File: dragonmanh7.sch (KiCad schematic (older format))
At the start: 145 parts, among them J1 USB_B, J10 Conn_02x12_Odd_Even, J11 Conn_02x05_Odd_Even, J12 VBAT+, J13 Conn_02x05_Odd_Even, J14 VBATG, J15 Conn_02x02_Odd_Even, J16 Conn_02x02_Odd_Even, J18 Conn_02x05_Odd_Even, J2 73725-0110BLF, J3 RJ45_Amphenol_RJMG1BD3B8K1ANR, J4 105162-0001, J5 Screw_Terminal_01x06, J6 Conn_02x12_Odd_Even, J7 USB_B, J8 Screw_Terminal_01x02, J9 Conn_02x12_Odd_Even, SW1 RESET, SW2 PC13, U1 STM32H743VITx, U10 USBLC6-2SC6, U12 TCAN332, U13 ISL83483, U14 MIC2005A, U2 LAN8742A-CZ-TR, U3 AZ1117CD-3.3TRG1, U5 S25FL127SABMFI101, U6 AP63205, U7 USBLC6-2SC6, U8 STM32F042F6Px, U9 USBLC6-2SC6, Y1 8MHz, Y2 32.768KHz, Y3 25MHz

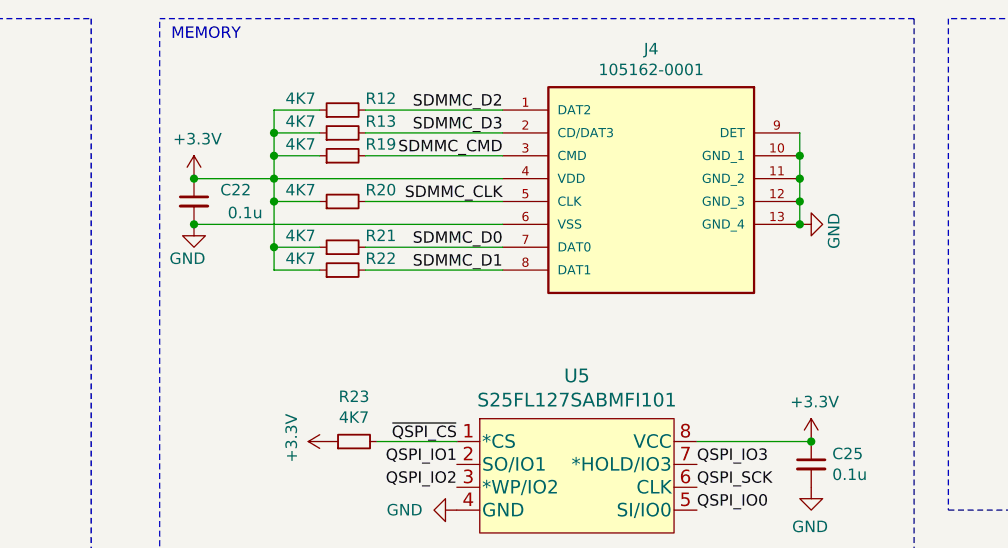
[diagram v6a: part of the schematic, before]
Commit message: Add ESD filters to uSD connector, improve routing
Signed-off-by: Martin Ribelotta <martinribelotta@gmail.com>
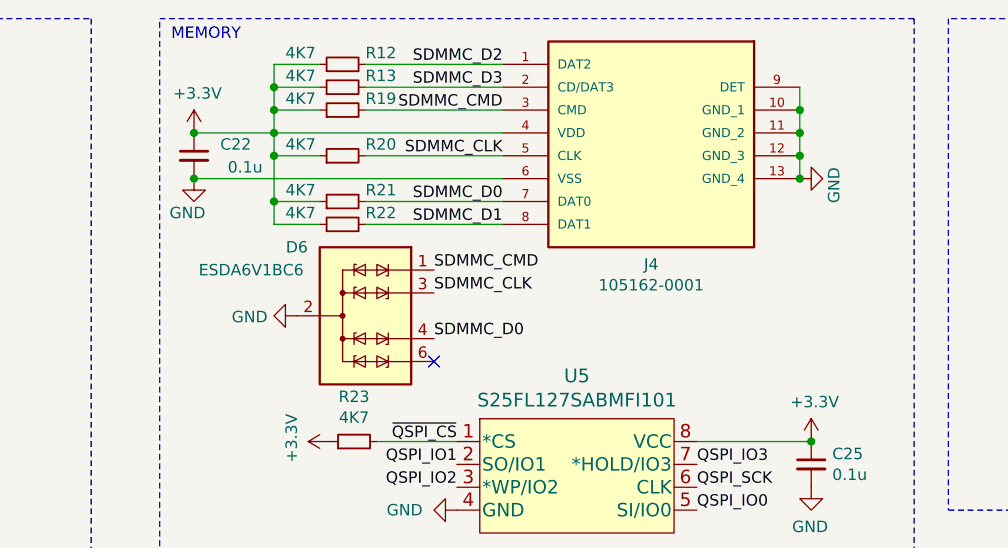
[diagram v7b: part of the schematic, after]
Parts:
- added D6: ESDA6V1BC6, Package_TO_SOT_SMD:SOT-23-6, symbol Power_Protection:ESDA6V1BC6
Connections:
- net GND: now also D6.2 (COM), D6.5 (COM)
- net SDMMC_CLK: now also D6.3 (TVS2)
- net SDMMC_CMD: now also D6.1 (TVS1)
- net SDMMC_D0: now also D6.4 (TVS3)
- no-connect marks 6 -> 7
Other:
- moved on the sheet: C22, J4, R12, R13, R19, R20, R21, R22
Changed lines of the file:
@@
 Text Label 1950 5150 2    50   ~ 0
 SDMMC_CMD
-Text Label 6550 1150 2    50   ~ 0
+Text Label 6550 950  2    50   ~ 0
 SDMMC_CMD
-Text Label 6550 1550 2    50   ~ 0
-SDMMC_D0
 Text Label 6550 1350 2    50   ~ 0
+SDMMC_D0
+Text Label 6550 1150 2    50   ~ 0
 SDMMC_CLK
 $Comp
 L Device:C_Small C22
 U 1 1 5C63370C
-P 5200 1350
-F 0 "C22" H 4950 1400 50  0000 L CNN
-F 1 "0.1u" H 4900 1300 50  0000 L CNN
-F 2 "Capacitor_SMD:C_0603_1608Metric" H 5200 1350 50  0001 C CNN
-F 3 "~" H 5200 1350 50  0001 C CNN
-F 4 "885012207098" H -300 0   50  0001 C CNN "manf#"
-	1    5200 1350
+P 5200 1150
+F 0 "C22" H 4950 1200 50  0000 L CNN
+F 1 "0.1u" H 4900 1100 50  0000 L CNN
+F 2 "Capacitor_SMD:C_0603_1608Metric" H 5200 1150 50  0001 C CNN
+F 3 "~" H 5200 1150 50  0001 C CNN
+F 4 "885012207098" H -300 -200 50  0001 C CNN "manf#"
+	1    5200 1150
 	-1   0    0    -1
 $EndComp
@@
 L power:+3.3V #PWR0122
 U 1 1 5C64A989
-P 5200 1250
-F 0 "#PWR0122" H 5200 1100 50  0001 C CNN
-F 1 "+3.3V" H 5215 1423 50  0000 C CNN
-F 2 "" H 5200 1250 50  0001 C CNN
-F 3 "" H 5200 1250 50  0001 C CNN
-	1    5200 1250
+P 5200 1050
+F 0 "#PWR0122" H 5200 900 50  0001 C CNN
+F 1 "+3.3V" H 5215 1223 50  0000 C CNN
+F 2 "" H 5200 1050 50  0001 C CNN
+F 3 "" H 5200 1050 50  0001 C CNN
+	1    5200 1050
 	1    0    0    -1
 $EndComp
-Connection ~ 5200 1250
+Connection ~ 5200 1050
 $Comp
 L power:GND #PWR0123
 U 1 1 5C65D44E
-P 5200 1450
-F 0 "#PWR0123" H 5200 1200 50  0001 C CNN
-F 1 "GND" H 5250 1300 50  0000 R CNN
-F 2 "" H 5200 1450 50  0001 C CNN
-F 3 "" H 5200 1450 50  0001 C CNN
-	1    5200 1450
+P 5200 1250
+F 0 "#PWR0123" H 5200 1000 50  0001 C CNN
+F 1 "GND" H 5250 1100 50  0000 R CNN
+F 2 "" H 5200 1250 50  0001 C CNN
+F 3 "" H 5200 1250 50  0001 C CNN
+	1    5200 1250
 	1    0    0    -1
 $EndComp
-Connection ~ 5200 1450
+Connection ~ 5200 1250
 $Comp
 L power:GND #PWR0124
 U 1 1 5C65D59B
-P 7850 1450
-F 0 "#PWR0124" H 7850 1200 50  0001 C CNN
-F 1 "GND" H 7900 1300 50  0000 R CNN
-F 2 "" H 7850 1450 50  0001 C CNN
-F 3 "" H 7850 1450 50  0001 C CNN
-	1    7850 1450
+P 7850 1250
+F 0 "#PWR0124" H 7850 1000 50  0001 C CNN
+F 1 "GND" H 7900 1100 50  0000 R CNN
+F 2 "" H 7850 1250 50  0001 C CNN
+F 3 "" H 7850 1250 50  0001 C CNN
+	1    7850 1250
 	0    -1   -1   0
 $EndComp
@@
 L Device:R_Small R12
 U 1 1 5D864354
-P 5850 950
-F 0 "R12" V 5900 850 50  0000 R CNN
-F 1 "4K7" V 5900 1200 50  0000 R CNN
-F 2 "Resistor_SMD:R_0603_1608Metric" H 5850 950 50  0001 C CNN
-F 3 "~" H 5850 950 50  0001 C CNN
-F 4 "CRGCQ0805J22R" H -2900 -1250 50  0001 C CNN "manf#"
-	1    5850 950
+P 5850 750
+F 0 "R12" V 5900 650 50  0000 R CNN
+F 1 "4K7" V 5900 1000 50  0000 R CNN
+F 2 "Resistor_SMD:R_0603_1608Metric" H 5850 750 50  0001 C CNN
+F 3 "~" H 5850 750 50  0001 C CNN
+F 4 "CRGCQ0805J22R" H -2900 -1450 50  0001 C CNN "manf#"
+	1    5850 750
 	0    -1   -1   0
 $EndComp
 Wire Wire Line
-	5200 1250 5550 1250
+	5200 1050 5550 1050
 Wire Wire Line
-	5200 1450 6550 1450
+	5200 1250 6550 1250
 $Comp
 L Device:R_Small R13
 U 1 1 5D8B50D6
-P 5850 1050
-F 0 "R13" V 5900 950 50  0000 R CNN
-F 1 "4K7" V 5900 1300 50  0000 R CNN
-F 2 "Resistor_SMD:R_0603_1608Metric" H 5850 1050 50  0001 C CNN
-F 3 "~" H 5850 1050 50  0001 C CNN
-F 4 "CRGCQ0805J22R" H -2900 -1150 50  0001 C CNN "manf#"
-	1    5850 1050
+P 5850 850
+F 0 "R13" V 5900 750 50  0000 R CNN
+F 1 "4K7" V 5900 1100 50  0000 R CNN
+F 2 "Resistor_SMD:R_0603_1608Metric" H 5850 850 50  0001 C CNN
+F 3 "~" H 5850 850 50  0001 C CNN
+F 4 "CRGCQ0805J22R" H -2900 -1350 50  0001 C CNN "manf#"
+	1    5850 850
 	0    -1   -1   0
 $EndComp
@@
 L Device:R_Small R19
 U 1 1 5D8B5413
+P 5850 950
+F 0 "R19" V 5900 850 50  0000 R CNN
+F 1 "4K7" V 5900 1200 50  0000 R CNN
+F 2 "Resistor_SMD:R_0603_1608Metric" H 5850 950 50  0001 C CNN
+F 3 "~" H 5850 950 50  0001 C CNN
+F 4 "CRGCQ0805J22R" H -2900 -1250 50  0001 C CNN "manf#"
+	1    5850 950
+	0    -1   -1   0
+$EndComp
+$Comp
+L Device:R_Small R20
+U 1 1 5D8B557E
 P 5850 1150
-F 0 "R19" V 5900 1050 50  0000 R CNN
+F 0 "R20" V 5900 1050 50  0000 R CNN
 F 1 "4K7" V 5900 1400 50  0000 R CNN
 F 2 "Resistor_SMD:R_0603_1608Metric" H 5850 1150 50  0001 C CNN
@@
 $EndComp
 $Comp
-L Device:R_Small R20
-U 1 1 5D8B557E
+L Device:R_Small R21
+U 1 1 5D8B584B
 P 5850 1350
-F 0 "R20" V 5900 1250 50  0000 R CNN
+F 0 "R21" V 5900 1250 50  0000 R CNN
 F 1 "4K7" V 5900 1600 50  0000 R CNN
 F 2 "Resistor_SMD:R_0603_1608Metric" H 5850 1350 50  0001 C CNN
@@
 $EndComp
 $Comp
-L Device:R_Small R21
-U 1 1 5D8B584B
-P 5850 1550
-F 0 "R21" V 5900 1450 50  0000 R CNN
-F 1 "4K7" V 5900 1800 50  0000 R CNN
-F 2 "Resistor_SMD:R_0603_1608Metric" H 5850 1550 50  0001 C CNN
-F 3 "~" H 5850 1550 50  0001 C CNN
-F 4 "CRGCQ0805J22R" H -2900 -650 50  0001 C CNN "manf#"
-	1    5850 1550
-	0    -1   -1   0
-$EndComp
-$Comp
 L Device:R_Small R22
 U 1 1 5D8B5B28
-P 5850 1650
-F 0 "R22" V 5900 1550 50  0000 R CNN
-F 1 "4K7" V 5900 1900 50  0000 R CNN
-F 2 "Resistor_SMD:R_0603_1608Metric" H 5850 1650 50  0001 C CNN
-F 3 "~" H 5850 1650 50  0001 C CNN
-F 4 "CRGCQ0805J22R" H -2900 -550 50  0001 C CNN "manf#"
-	1    5850 1650
+P 5850 1450
+F 0 "R22" V 5900 1350 50  0000 R CNN
+F 1 "4K7" V 5900 1700 50  0000 R CNN
+F 2 "Resistor_SMD:R_0603_1608Metric" H 5850 1450 50  0001 C CNN
+F 3 "~" H 5850 1450 50  0001 C CNN
+F 4 "CRGCQ0805J22R" H -2900 -750 50  0001 C CNN "manf#"
+	1    5850 1450
 	0    -1   -1   0
 $EndComp
 Wire Wire Line
-	5950 1650 6550 1650
-Wire Wire Line
-	6550 1550 5950 1550
+	5950 1450 6550 1450
 Wire Wire Line
-	5950 1350 6550 1350
+	6550 1350 5950 1350
 Wire Wire Line
-	6550 1150 5950 1150
-Wire Wire Line
-	5950 1050 6550 1050
+	5950 1150 6550 1150
 Wire Wire Line
 	6550 950  5950 950
 Wire Wire Line
-	5750 950  5550 950
+	5950 850  6550 850
 Wire Wire Line
-	5550 950  5550 1050
+	6550 750  5950 750
 Wire Wire Line
-	5550 1650 5750 1650
+	5750 750  5550 750
 Wire Wire Line
-	5750 1550 5550 1550
-Connection ~ 5550 1550
+	5550 750  5550 850
 Wire Wire Line
-	5550 1550 5550 1650
+	5550 1450 5750 1450
 Wire Wire Line
 	5750 1350 5550 1350
 Connection ~ 5550 1350
 Wire Wire Line
-	5550 1350 5550 1550
+	5550 1350 5550 1450
 Wire Wire Line
 	5750 1150 5550 1150
 Connection ~ 5550 1150
 Wire Wire Line
-	5550 1150 5550 1250
+	5550 1150 5550 1350
 Wire Wire Line
-	5750 1050 5550 1050
-Connection ~ 5550 1050
+	5750 950  5550 950
+Connection ~ 5550 950
 Wire Wire Line
-	5550 1050 5550 1150
-Connection ~ 5550 1250
+	5550 950  5550 1050
+Wire Wire Line
+	5750 850  5550 850
+Connection ~ 5550 850
+Wire Wire Line
+	5550 850  5550 950
+Connection ~ 5550 1050
 Wire Wire Line
-	5550 1250 6550 1250
+	5550 1050 6550 1050
 Wire Wire Line
-	5550 1250 5550 1350
-Text Label 6550 1650 2    50   ~ 0
+	5550 1050 5550 1150
+Text Label 6550 1450 2    50   ~ 0
 SDMMC_D1
-Text Label 6550 950  2    50   ~ 0
+Text Label 6550 750  2    50   ~ 0
 SDMMC_D2
-Text Label 6550 1050 2    50   ~ 0
+Text Label 6550 850  2    50   ~ 0
 SDMMC_D3
 $Comp
@@
 L 105162-0001:105162-0001 J4
 U 1 1 5FA74A6B
-P 6550 950
-F 0 "J4" H 7200 1217 50  0000 C CNN
-F 1 "105162-0001" H 7200 1126 50  0000 C CNN
-F 2 "footprints:105162-0001" H 6550 950 50  0001 L BNN
-F 3 "" H 6550 950 50  0001 L BNN
-F 4 "https://www.mouser.co.uk/ProductDetail/Molex/105162-0001?qs=1fNsfHe5VsK8daqlgKxZfQ%3D%3D" H 6550 950 50  0001 L BNN "MOUSER_PRICE-STOCK"
-F 5 "105162-0001" H 6550 950 50  0001 L BNN "MANUFACTURER_PART_NUMBER"
-F 6 "538-105162-0001" H 6550 950 50  0001 L BNN "MOUSER_PART_NUMBER"
-F 7 "Molex" H 6550 950 50  0001 L BNN "MANUFACTURER_NAME"
-F 8 "Memory Card Connectors 1.45H MICRO SD HEADER WITH D/C PIN" H 6550 950 50  0001 L BNN "DESCRIPTION"
-F 9 "mm" H 6550 950 50  0001 L BNN "HEIGHT"
-	1    6550 950
+P 6550 750
+F 0 "J4" H 7200 -125 50  0000 C CNN
+F 1 "105162-0001" H 7200 -216 50  0000 C CNN
+F 2 "footprints:105162-0001" H 6550 750 50  0001 L BNN
+F 3 "" H 6550 750 50  0001 L BNN
+F 4 "https://www.mouser.co.uk/ProductDetail/Molex/105162-0001?qs=1fNsfHe5VsK8daqlgKxZfQ%3D%3D" H 6550 750 50  0001 L BNN "MOUSER_PRICE-STOCK"
+F 5 "105162-0001" H 6550 750 50  0001 L BNN "MANUFACTURER_PART_NUMBER"
+F 6 "538-105162-0001" H 6550 750 50  0001 L BNN "MOUSER_PART_NUMBER"
+F 7 "Molex" H 6550 750 50  0001 L BNN "MANUFACTURER_NAME"
+F 8 "Memory Card Connectors 1.45H MICRO SD HEADER WITH D/C PIN" H 6550 750 50  0001 L BNN "DESCRIPTION"
+F 9 "mm" H 6550 750 50  0001 L BNN "HEIGHT"
+	1    6550 750
 	1    0    0    -1
 $EndComp
 Wire Wire Line
-	7850 1150 7850 1250
-Connection ~ 7850 1450
+	7850 950  7850 1050
 Connection ~ 7850 1250
-Wire Wire Line
-	7850 1250 7850 1350
-Connection ~ 7850 1350
-Wire Wire Line
-	7850 1350 7850 1450
+Connection ~ 7850 1050
 Wire Wire Line
 	7850 1050 7850 1150
 Connection ~ 7850 1150
+Wire Wire Line
+	7850 1150 7850 1250
+Wire Wire Line
+	7850 850  7850 950
+Connection ~ 7850 950
 $Comp
 L Connector:USB_B J7
@@
 Text Label 3750 6350 0    50   ~ 0
 32K-
+Text Label 6250 1950 0    50   ~ 0
+SDMMC_D0
+Text Label 6250 1750 0    50   ~ 0
+SDMMC_CLK
+Text Label 6250 1650 0    50   ~ 0
+SDMMC_CMD
+$Comp
+L power:GND #PWR030
+U 1 1 5FB24FDD
+P 5650 1850
+F 0 "#PWR030" H 5650 1600 50  0001 C CNN
+F 1 "GND" V 5655 1722 50  0000 R CNN
+F 2 "" H 5650 1850 50  0001 C CNN
+F 3 "" H 5650 1850 50  0001 C CNN
+	1    5650 1850
+	0    1    1    0
+$EndComp
+$Comp
+L Power_Protection:ESDA6V1BC6 D6
+U 1 1 5FBA8203
+P 5950 1850
+F 0 "D6" V 5650 1550 50  0000 C CNN
+F 1 "ESDA6V1BC6" V 5750 1350 50  0000 C CNN
+F 2 "Package_TO_SOT_SMD:SOT-23-6" H 5950 1500 50  0001 C CNN
+F 3 "http://www.st.com/content/ccc/resource/technical/document/datasheet/21/07/21/e3/a8/df/42/a2/CD00001906.pdf/files/CD00001906.pdf/jcr:content/translations/en.CD00001906.pdf" V 5950 1850 50  0001 C CNN
+	1    5950 1850
+	0    1    1    0
+$EndComp
+NoConn ~ 6250 2050
 $EndSCHEMATC

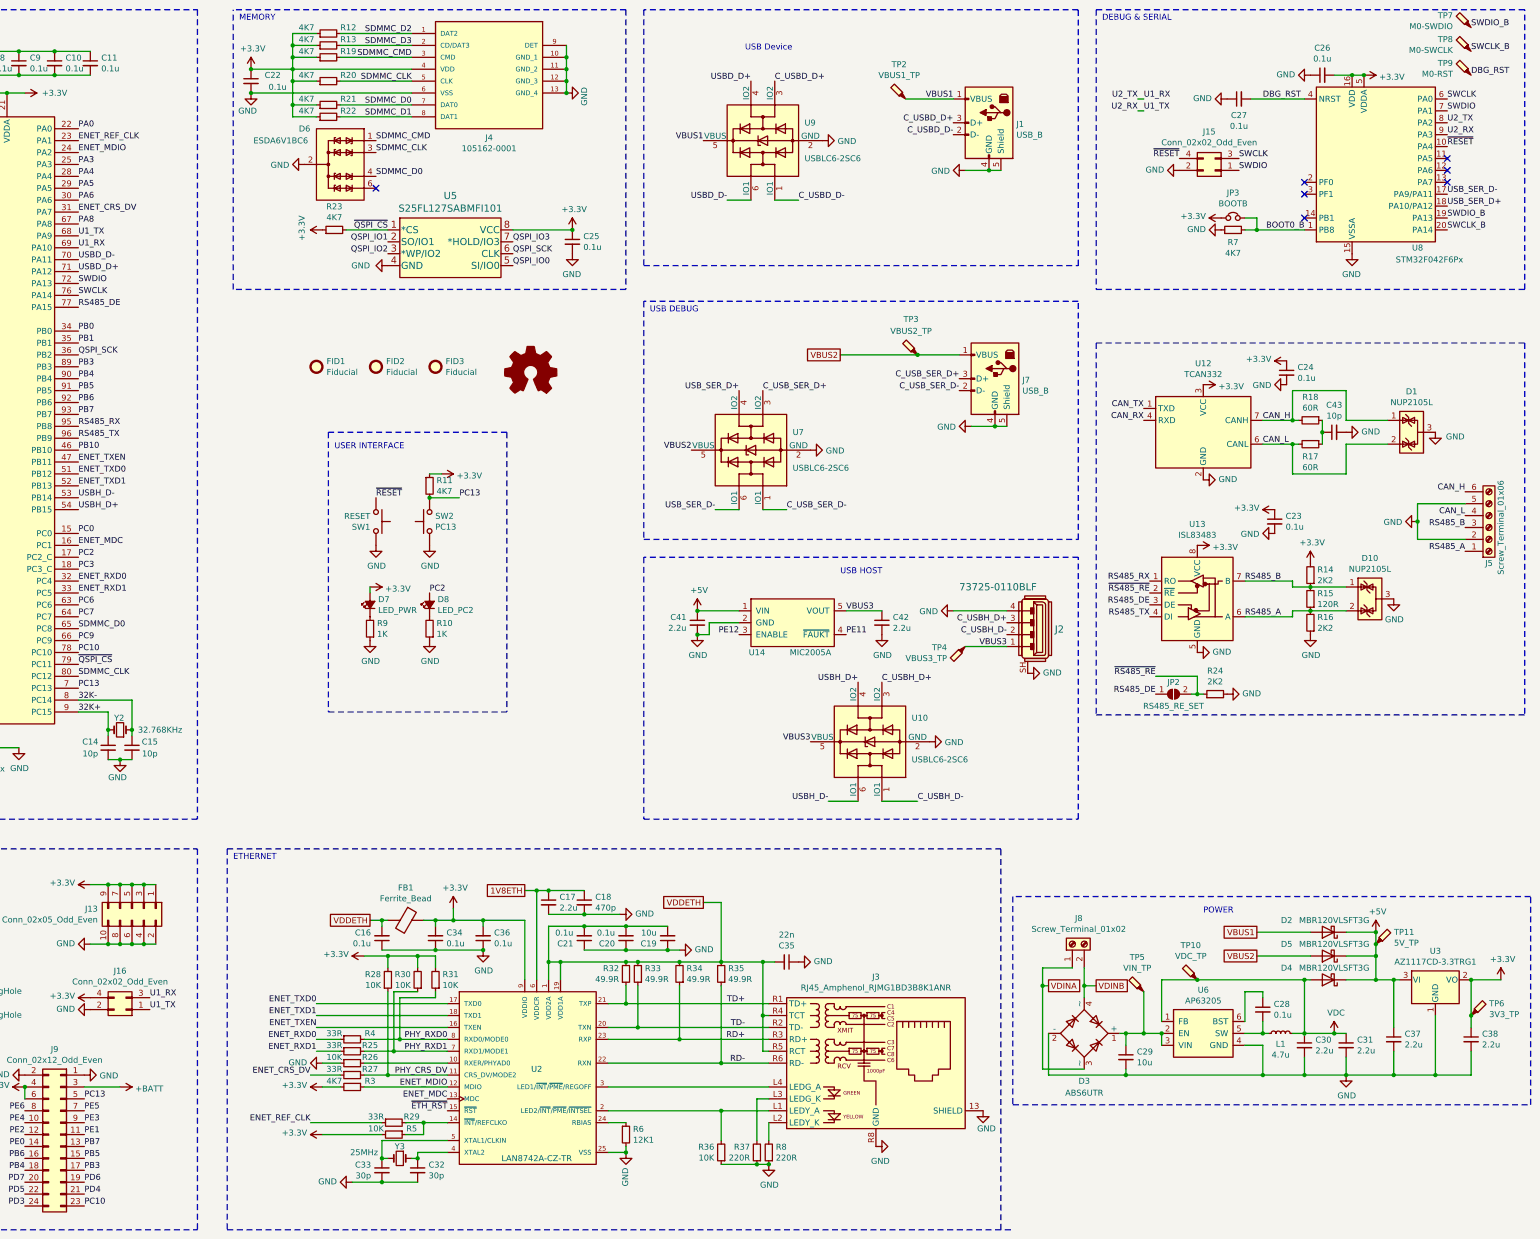
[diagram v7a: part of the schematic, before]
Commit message: Minor changes, add uSD DET on PC10
Signed-off-by: Martin Ribelotta <martinribelotta@gmail.com>
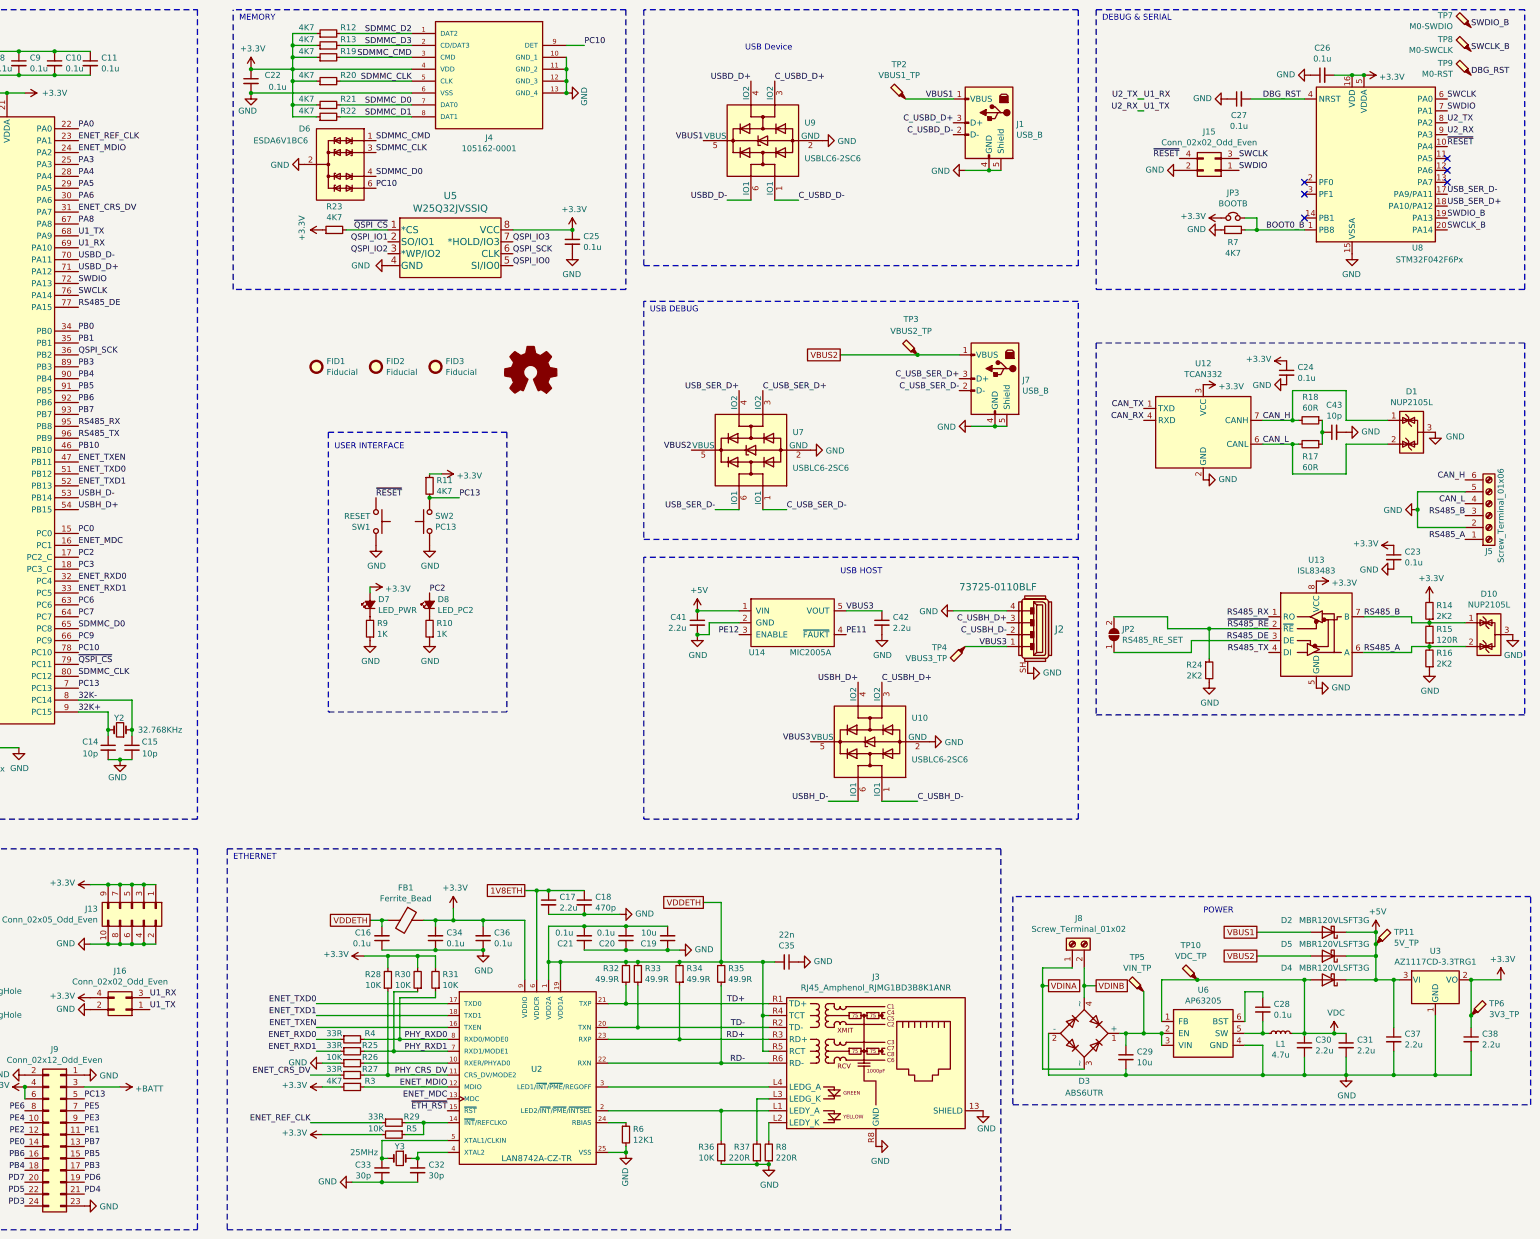
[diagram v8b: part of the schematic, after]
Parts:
- U5: value S25FL127SABMFI101 -> W25Q32JVSSIQ; manf# S25FL127SABMFI101 -> W25Q32JVSSIQ
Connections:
- net GND: now also J9.23 (Pin_23); no longer J4.9 (DET)
- net PC10: now also D6.6 (TVS4), J4.9 (DET); no longer J9.23 (Pin_23)
- no-connect marks 7 -> 6
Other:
- moved on the sheet: C23, D10, J5, JP2, R14, R15, R16, R24, U13
